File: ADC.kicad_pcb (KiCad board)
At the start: 2 copper layers, 148 parts, among them P1 CONN_6, P10 CONN_2, P11 CONN_2, P12 CONN_2, P13 CONN_4, P14 CONN_2, P15 CONN_2, P16 CONN_2, P17 CONN_4, P2 CONN_6, P3 CONN_6, P4 CONN_6, P5 CONN_1, P6 CONN_2, P7 CONN_2, P8 CONN_2, P9 CONN_2, Q1 BD241A, Q2 BD241A, Q3 BD242, T1 TRIAD-FS16-400-C2, T2 TRIAD-FS48-750-C2, U1 OPA209-SOT23, U12 MC7805C, U13 LM7818CT, U14 LM7918CT, U15 LME49740, U16 LME49740, U2 OPA209-SOT23, U3 OPA209-SOT23, U4 2N6507, U5 2N6507, U6 2N6507, U7 REF02, U8 2N6507, U9 OPA209-SOT23

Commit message: Changed to use the fixed IEC socket device; the PSU netlist should now be (more) correct.
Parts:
- added C21: C, Capacitors_ThroughHole:Capacitor12MMDiscRM7.75, F.Cu at (56.3, 104.6)
- added C22: C, Capacitors_ThroughHole:Capacitor12MMDiscRM7.75, F.Cu at (43.3, 104.6)
- added F1: FUSE, Oddities:Dummy_Empty, F.Cu at (102.6, 105.8)
- added J1: RCA, Oddities:Dummy_Empty, F.Cu at (575.6, 90.6)
- added J2: RCA, Oddities:Dummy_Empty, F.Cu at (623.8, 62.6)
- added J3: IEC-C13-SOCKET, Oddities:Dummy_Empty, F.Cu at (28.0, 103.2)
- added P18: CONN_1, Connect:1pin, F.Cu at (111.8, 26.7)
- added P19: CONN_1, Connect:1pin, F.Cu at (90.2, -113.0)
- added P20: CONN_1, Connect:1pin, F.Cu at (90.2, -123.2)
- added P21: CONN_1, Connect:1pin, F.Cu at (88.9, -143.5)
- added P22: CONN_1, Connect:1pin, F.Cu at (90.2, -154.9)
- added R21: R, Resistors_ThroughHole:Resistor_Horizontal_RM15mm, F.Cu at (96.4, 84.2)
- added R22: R, Resistors_ThroughHole:Resistor_Horizontal_RM15mm, F.Cu at (137.3, 48.1)
- added U10: P0300ECL, Housings_TO-92:TO-92-Free-inline-wide, F.Cu at (93.1, 96.8)
- added U11: P0300ECL, Housings_TO-92:TO-92-Free-inline-wide, F.Cu at (127.1, 62.3)
- P14, P15, P16, P6, P7: footprint Sockets_MOLEX_KK-System:Socket_MOLEX-KK-RM2-54mm_Lock_2pin_straight -> Oddities:Dummy_Empty
- P17: footprint Sockets_MOLEX_KK-System:Socket_MOLEX-KK-RM2-54mm_Lock_4pin_straight -> Oddities:Dummy_Empty
- P2, P3: footprint Sockets_MOLEX_KK-System:Socket_MOLEX-KK-RM2-54mm_Lock_6pin_straight -> Oddities:Dummy_Empty
- moved R33 477.1 mm to (601.5, 6.55)
- moved D20 472.3 mm to (614.1, 6.53)
- moved D23 460.6 mm to (601.0, 27.5)
- moved C40 455.2 mm to (623.2, 6.35)
- moved R34 450.0 mm to (563.4, 27.5)
- moved R41 449.9 mm to (588.8, 6.55)
- moved R39 439.4 mm to (563.4, 6.55)
- moved R50 434.2 mm to (537.8, 6.55)
- moved R46 428.5 mm to (576.2, 6.55)
- moved R48 428.4 mm to (550.6, 6.55)
- moved R44 422.8 mm to (550.6, 38.0)
- moved P12 421.8 mm to (597.9, 64.8)
- moved P8 421.8 mm to (617.4, 64.8)
- moved C41 417.2 mm to (584.5, 47.1)
- moved R32 417.2 mm to (588.7, 17.0)
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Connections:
- T1 pad 1: Net-(J3-Pad~) -> Net-(J3-Pad1)
- T1 pad 2: Net-(J3-Pad~) -> Net-(J3-Pad2)
- T1 pad 3: Net-(J3-Pad~) -> Net-(J3-Pad3)
- T1 pad 4: Net-(J3-Pad~) -> Net-(J3-Pad4)
- T2 pad 1: Net-(J3-Pad~) -> Net-(J3-Pad1)
- T2 pad 2: Net-(J3-Pad~) -> Net-(J3-Pad2)
- T2 pad 3: Net-(J3-Pad~) -> Net-(J3-Pad3)
- T2 pad 4: Net-(J3-Pad~) -> Net-(J3-Pad4)

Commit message: A lot of routing, some parts changes:   * Added snubber C/RC snubbers to transformer secondaries.   * Changed PSU OA from OPA209 to OPA27.   * Routed external PSU.   * Mostly done routing internal circuits.  Just need to get everything together.   * Changed digital transformer to a more appropriately-specced one.
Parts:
- added C44: 470n, Capacitors_ThroughHole:Capacitor3MMDiscRM2.5, F.Cu at (245.4, 51.1)
- added C45: 470n, Capacitors_ThroughHole:Capacitor3MMDiscRM2.5, F.Cu at (248.0, 66.4)
- added HS: Heatsink_Fischer_SK104-STC-STIC_35x13mm_2xDrill2.5mm, Heatsinks:Heatsink_Fischer_SK104-STC-STIC_35x13mm_2xDrill2.5mm, F.Cu at (128.2, 59.9)
- added HS: Heatsink_Fischer_SK104-STC-STIC_35x13mm_2xDrill2.5mm, Heatsinks:Heatsink_Fischer_SK104-STC-STIC_35x13mm_2xDrill2.5mm, F.Cu at (41.9, 48.4)
- added HS: Heatsink_Fischer_SK104-STC-STIC_35x13mm_2xDrill2.5mm, Heatsinks:Heatsink_Fischer_SK104-STC-STIC_35x13mm_2xDrill2.5mm, F.Cu at (78.7, 48.4)
- added HS: Heatsink_Fischer_SK104-STC-STIC_35x13mm_2xDrill2.5mm, Heatsinks:Heatsink_Fischer_SK104-STC-STIC_35x13mm_2xDrill2.5mm, F.Cu at (231.5, 114.0)
- added HS: Heatsink_Fischer_SK104-STC-STIC_35x13mm_2xDrill2.5mm, Heatsinks:Heatsink_Fischer_SK104-STC-STIC_35x13mm_2xDrill2.5mm, F.Cu at (430.5, 181.6)
- added HS: Heatsink_Fischer_SK104-STC-STIC_35x13mm_2xDrill2.5mm, Heatsinks:Heatsink_Fischer_SK104-STC-STIC_35x13mm_2xDrill2.5mm, F.Cu at (177.5, 114.0)
- added MH: MountingHole_5mm_RevA_Date21Jun2010, Mounting_Holes:MountingHole_5mm, F.Cu at (32.5, 35.0)
- added MH: MountingHole_5mm_RevA_Date21Jun2010, Mounting_Holes:MountingHole_5mm, F.Cu at (127.5, 35.0)
- added MH: MountingHole_5mm_RevA_Date21Jun2010, Mounting_Holes:MountingHole_5mm, F.Cu at (32.5, 180.0)
- added MH: MountingHole_5mm_RevA_Date21Jun2010, Mounting_Holes:MountingHole_5mm, F.Cu at (127.5, 180.0)
- added MH: MountingHole_5mm_RevA_Date21Jun2010, Mounting_Holes:MountingHole_5mm, F.Cu at (100.0, 90.0)
- added Sym: Symbol_Highvoltage_Type2_CopperTop_Small, Footprint_Symbols:Symbol_Highvoltage_Type2_CopperTop_Small, B.Cu at (35.6, 138.4)
- added Sym: Symbol_Danger_CopperTop_Big, Footprint_Symbols:Symbol_Danger_CopperTop_Big, B.Cu at (55.9, 137.2)
- C21: value C -> 150n; footprint Capacitors_ThroughHole:Capacitor12MMDiscRM7.75 -> Capacitors_ThroughHole:Capacitor18x6RM15
- C22: value C -> 10n; footprint Capacitors_ThroughHole:Capacitor12MMDiscRM7.75 -> Capacitors_ThroughHole:Capacitor13x4RM10
- C23: value 2700u -> 150n; footprint Capacitors_ThroughHole:Capacitor16x25RM7.5 -> Capacitors_ThroughHole:Capacitor18x6RM15
- C24: value 2700u -> 10n; footprint Capacitors_ThroughHole:Capacitor16x25RM7.5 -> Capacitors_ThroughHole:Capacitor13x4RM10
- C28, C29: value 470n -> 2700u; footprint Capacitors_ThroughHole:Capacitor3MMDiscRM2.5 -> Capacitors_ThroughHole:Capacitor16x25RM7.5
- C31, C32: value 1u -> 470n; footprint Capacitors_ThroughHole:Capacitor5x6RM2.5 -> Capacitors_ThroughHole:Capacitor3MMDiscRM2.5
- C34, C35: value 6.2n -> 1u; footprint Capacitors_ThroughHole:Capacitor18x7RM15 -> Capacitors_ThroughHole:Capacitor5x6RM2.5
- C36, C37: value 22u -> 6.2n; footprint Capacitors_ThroughHole:Capacitor5x11RM2.5 -> Capacitors_ThroughHole:Capacitor18x7RM15
- C38, C39: value 47u -> 22u; footprint Capacitors_Elko_ThroughHole:Elko_vert_DM5_RM2 -> Capacitors_ThroughHole:Capacitor5x11RM2.5
- C40, C41: value 470n -> 47u; footprint Capacitors_ThroughHole:Capacitor3MMDiscRM2.5 -> Capacitors_Elko_ThroughHole:Elko_vert_DM5_RM2
- T1: value TRIAD-FS16-400-C2 -> TRIAD-FS20-300-C2
- U1, U2, U3, U9: value OPA209-SOT23 -> OPA27; footprint SMD_Packages:SOT23-5 -> Sockets_DIP:DIP-8__300_ELL
- moved J3 767.8 mm to (793.7, 160.3)
- moved F1 687.6 mm to (787.5, 167.1)
- moved C40 446.9 mm to (180.3, 66.0)
- moved C35 446.3 mm to (45.7, 63.7), turned to 270 degrees
- moved C42 423.9 mm to (189.2, 64.8)
- moved D19 421.2 mm to (180.3, 30.5), turned to 180 degrees
- moved P8 415.1 mm to (202.6, 80.0), turned to 90 degrees
- moved P5 411.9 mm to (177.8, 153.0)
- moved C43 410.8 mm to (186.7, 49.5)
- moved R32 409.4 mm to (180.3, 45.7)
- moved C34 407.4 mm to (82.5, 63.7), turned to 90 degrees
- moved R33 406.9 mm to (196.8, 49.5)
- moved R31 396.0 mm to (180.3, 41.9)
- moved D17 395.5 mm to (180.3, 34.3)
- moved P10 395.4 mm to (202.6, 69.8), turned to 90 degrees
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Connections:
- net Net-(J3-Pad1) renamed /PSU-external/PA1
- net Net-(J3-Pad2) renamed /PSU-external/PA2
- net Net-(J3-Pad3) renamed /PSU-external/PB1
- net Net-(J3-Pad4) renamed /PSU-external/PB2
- C21 pad 1: Net-(C21-Pad1) -> /PSU-external/SEC4
- C21 pad 2: Net-(C21-Pad2) -> /PSU-external/SEC3
- C22 pad 1: Net-(C22-Pad1) -> /PSU-external/SEC6
- C22 pad 2: Net-(C22-Pad2) -> /PSU-external/SEC3
- C23 pad 1: Net-(C23-Pad1) -> /PSU-external/SEC2
- C23 pad 2: /PSU-external/AGND_EXT -> /PSU-external/SEC1
- C24 pad 1: /PSU-external/AGND_EXT -> /PSU-external/SEC7
- C24 pad 2: Net-(C24-Pad2) -> /PSU-external/SEC1
- C25 pad 2: /PSU-external/DGND_EXT -> /PSU-external/AGND_EXT
- C26 pad 1: Net-(C23-Pad1) -> /PSU-external/AGND_EXT
- C26 pad 2: /PSU-external/AGND_EXT -> Net-(C26-Pad2)
- C27 pad 1: /PSU-external/AGND_EXT -> Net-(C27-Pad1)
- C27 pad 2: Net-(C24-Pad2) -> /PSU-external/DGND_EXT
- C28 pad 2: /PSU-external/DGND_EXT -> /PSU-external/AGND_EXT
- C29 pad 1: Net-(C23-Pad1) -> /PSU-external/AGND_EXT
- C29 pad 2: /PSU-external/AGND_EXT -> Net-(C26-Pad2)
- C30 pad 1: /PSU-external/AGND_EXT -> Net-(C27-Pad1)
- C30 pad 2: Net-(C24-Pad2) -> /PSU-external/DGND_EXT
- C31 pad 1: /PSU-external/+5V_EXT -> Net-(C25-Pad1)
- C31 pad 2: /PSU-external/DGND_EXT -> /PSU-external/AGND_EXT
- C32 pad 1: /PSU-external/+18V_EXT -> /PSU-external/AGND_EXT
- C32 pad 2: /PSU-external/AGND_EXT -> Net-(C26-Pad2)
- C33 pad 1: /PSU-external/AGND_EXT -> /PSU-external/+5V_EXT
- C33 pad 2: /PSU-external/-18V_EXT -> /PSU-external/DGND_EXT
- C34 pad 1: Net-(C34-Pad1) -> /PSU-external/+18V_EXT
- C34 pad 2: /Clipper/AGND -> /PSU-external/AGND_EXT
- C35 pad 1: Net-(C35-Pad1) -> /PSU-external/AGND_EXT
- C35 pad 2: /Clipper/AGND -> /PSU-external/-18V_EXT
- C36 pad 1: Net-(C34-Pad1) -> Net-(C36-Pad1)
- C36 pad 2: Net-(C36-Pad2) -> /Clipper/AGND
- C37 pad 1: Net-(C35-Pad1) -> Net-(C37-Pad1)
- C37 pad 2: Net-(C37-Pad2) -> /Clipper/AGND
- C38 pad 1: /Clipper/LIN -> Net-(C36-Pad1)
- C39 pad 1: /Clipper/RIN -> Net-(C37-Pad1)
- C40 pad 1: /Clipper/+15V -> /Clipper/LIN
- C40 pad 2: /Clipper/AGND -> Net-(C40-Pad2)
- C41 pad 1: /Clipper/AGND -> /Clipper/RIN
- C41 pad 2: /Clipper/-15V -> Net-(C41-Pad2)
- D10 pad 2: Net-(D10-Pad2) -> /PSU-external/SEC4
- D11 pad 1: Net-(C22-Pad2) -> /PSU-external/SEC1
- D11 pad 2: Net-(C23-Pad1) -> Net-(C25-Pad1)
- D12 pad 1: Net-(C24-Pad2) -> Net-(C26-Pad2)
- D12 pad 2: Net-(C22-Pad2) -> /PSU-external/SEC1
- D13 pad 2: Net-(C25-Pad1) -> Net-(C27-Pad1)
- D14 pad 2: Net-(C23-Pad1) -> Net-(C25-Pad1)
- D15 pad 1: Net-(C24-Pad2) -> Net-(C26-Pad2)
- D19 pad 1: Net-(D17-Pad2) -> Net-(D19-Pad1)
- D19 pad 2: Net-(D19-Pad2) -> Net-(D17-Pad1)
- D23 pad 1: Net-(D21-Pad2) -> Net-(D23-Pad1)
- D23 pad 2: Net-(D23-Pad2) -> Net-(D21-Pad1)
- D5 pad 1: Net-(C21-Pad2) -> /PSU-external/SEC3
- D5 pad 2: Net-(C25-Pad1) -> Net-(C27-Pad1)
- D6 pad 2: Net-(C21-Pad2) -> /PSU-external/SEC3
- D7 pad 1: Net-(D7-Pad1) -> /PSU-external/SEC2
- D7 pad 2: Net-(C23-Pad1) -> Net-(C25-Pad1)
- D8 pad 1: Net-(C24-Pad2) -> Net-(C26-Pad2)
- D8 pad 2: Net-(D7-Pad1) -> /PSU-external/SEC2
- D9 pad 1: Net-(D10-Pad2) -> /PSU-external/SEC4
- D9 pad 2: Net-(C25-Pad1) -> Net-(C27-Pad1)
- P1 pad 1: /PSU-external/SAF_GND -> /PSU-external/+5V_EXT
- P1 pad 2: /PSU-external/+5V_EXT -> /PSU-external/DGND_EXT
- P1 pad 3: /PSU-external/DGND_EXT -> /PSU-external/SAF_GND
- P4 pad 1: Net-(P4-Pad1) -> /PSU-internal/+5V
- P4 pad 2: /PSU-internal/+5V -> /PSU-internal/DGND
- P4 pad 3: /PSU-internal/DGND -> Net-(P4-Pad3)
- P5 pad 1: Net-(P4-Pad1) -> Net-(P4-Pad3)
- R21 pad 1: Net-(C21-Pad1) -> /PSU-external/SEC6
- R21 pad 2: Net-(D10-Pad2) -> /PSU-external/SEC4
- R22 pad 1: Net-(C22-Pad1) -> /PSU-external/SEC7
- R22 pad 2: Net-(D7-Pad1) -> /PSU-external/SEC2
- R23 pad 2: Net-(C34-Pad1) -> Net-(C36-Pad1)
- R24 pad 2: Net-(C35-Pad1) -> Net-(C37-Pad1)
- R25 pad 1: Net-(C34-Pad1) -> Net-(C36-Pad1)
- R26 pad 1: Net-(C35-Pad1) -> Net-(C37-Pad1)
- R27 pad 1: Net-(C36-Pad2) -> Net-(C38-Pad2)
- R28 pad 1: Net-(C37-Pad2) -> Net-(C39-Pad2)
- R32 pad 2: Net-(D17-Pad1) -> Net-(D17-Pad2)
- R34 pad 2: Net-(D17-Pad1) -> Net-(D17-Pad2)
- R36 pad 1: Net-(D17-Pad1) -> Net-(D17-Pad2)
- R36 pad 2: Net-(D19-Pad2) -> Net-(D19-Pad1)
- R39 pad 1: Net-(D19-Pad2) -> Net-(D19-Pad1)
- R42 pad 2: Net-(D21-Pad1) -> Net-(D21-Pad2)
- R44 pad 2: Net-(D21-Pad1) -> Net-(D21-Pad2)
- R46 pad 1: Net-(D21-Pad1) -> Net-(D21-Pad2)
- R46 pad 2: Net-(D23-Pad2) -> Net-(D23-Pad1)
- R49 pad 1: Net-(D23-Pad2) -> Net-(D23-Pad1)
- T1 pad 5: Net-(C21-Pad2) -> /PSU-external/SEC3
- T1 pad 6: Net-(T1-Pad6) -> /PSU-external/SEC4
- T1 pad 7: Net-(T1-Pad6) -> /PSU-external/SEC3
- T1 pad 8: Net-(D10-Pad2) -> /PSU-external/SEC4
- T2 pad 5: Net-(C22-Pad2) -> /PSU-external/SEC1
- T2 pad 8: Net-(D7-Pad1) -> /PSU-external/SEC2
- U1 pad 1: Net-(R11-Pad2) -> Net-(U1-Pad1)
- U1 pad 2: /Clipper/AGND -> Net-(C4-Pad2)
- U1 pad 4: Net-(C4-Pad2) -> /PSU-internal/-18V_EXT
- U1 pad 5: /PSU-internal/+18V_EXT -> (no net)
- U10 pad 1: Net-(T1-Pad6) -> /PSU-external/SEC3
- U12 pad 1: Net-(C25-Pad1) -> Net-(C27-Pad1)
- U13 pad 1: Net-(C23-Pad1) -> Net-(C25-Pad1)
- U14 pad 2: Net-(C24-Pad2) -> Net-(C26-Pad2)
- U15 pad 1: Net-(C38-Pad2) -> Net-(C40-Pad2)
- U15 pad 13: Net-(R37-Pad2) -> Net-(D17-Pad2)
- U15 pad 14: /Clipper/LOUT -> Net-(D17-Pad1)
- U15 pad 2: Net-(C38-Pad2) -> Net-(C40-Pad2)
- U15 pad 3: Net-(C36-Pad2) -> Net-(C38-Pad2)
- U15 pad 6: Net-(D17-Pad1) -> Net-(R37-Pad2)
- U15 pad 7: Net-(D17-Pad2) -> /Clipper/LOUT
- U16 pad 1: Net-(C39-Pad2) -> Net-(C41-Pad2)
- U16 pad 13: Net-(R47-Pad2) -> Net-(D21-Pad2)
- U16 pad 14: /Clipper/ROUT -> Net-(D21-Pad1)
- U16 pad 2: Net-(C39-Pad2) -> Net-(C41-Pad2)
- U16 pad 3: Net-(C37-Pad2) -> Net-(C39-Pad2)
- U16 pad 6: Net-(D21-Pad1) -> Net-(R47-Pad2)
- U16 pad 7: Net-(D21-Pad2) -> /Clipper/ROUT
- U2 pad 1: Net-(R12-Pad2) -> Net-(U2-Pad1)
- U2 pad 2: /Clipper/AGND -> Net-(C5-Pad2)
- U2 pad 4: Net-(C5-Pad2) -> /PSU-internal/-18V_EXT
- U2 pad 5: /PSU-internal/+18V_EXT -> (no net)
- U3 pad 1: Net-(R13-Pad2) -> Net-(U3-Pad1)
- U3 pad 2: /PSU-internal/-18V_EXT -> Net-(C6-Pad1)
- U3 pad 4: Net-(C6-Pad1) -> /PSU-internal/-18V_EXT
- U3 pad 5: /Clipper/AGND -> (no net)
- U9 pad 1: /PSU-internal/VREF- -> Net-(U9-Pad1)
- U9 pad 2: /PSU-internal/-18V_EXT -> Net-(R18-Pad1)
- U9 pad 4: Net-(R18-Pad1) -> /PSU-internal/-18V_EXT
- U9 pad 5: /PSU-internal/+18V_EXT -> (no net)
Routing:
- net /PSU-external/AGND_EXT: track 0.00 -> 287.6 mm, vias 0 -> 4
- net /PSU-external/SAF_GND: track 0.00 -> 191.5 mm
- net /PSU-external/PA1: track 0.00 -> 147.9 mm
- net /PSU-external/DGND_EXT: track 0.00 -> 122.7 mm
- net Net-(C26-Pad2): track 0.00 -> 119.6 mm
- net Net-(C25-Pad1): track 0.00 -> 109.4 mm
- net /PSU-external/PA2: track 0.00 -> 105.2 mm
- net /Clipper/+15V: track 0.00 -> 97.3 mm
- net /PSU-external/+5V_EXT: track 0.00 -> 85.1 mm
- net /PSU-internal/-18V_EXT: track 0.00 -> 82.6 mm
- net /PSU-external/SEC3: track 0.00 -> 80.8 mm
- net /PSU-external/PB1: track 0.00 -> 78.8 mm
- net /PSU-internal/+18V_EXT: track 0.00 -> 78.3 mm
- net /Clipper/-15V: track 0.00 -> 78.1 mm
- net Net-(C27-Pad1): track 0.00 -> 75.6 mm
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- added copper zone on B.Cu, net /PSU-external/SAF_GND
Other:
- board outline added: 247.5 x 165 mm
- net class Default: trace_width 0.254 -> 1
- net class HighVoltage added: clearance 1, trace_width 2, via_dia 0.889, via_drill 0.635
- net class Power added: clearance 0.254, trace_width 1, via_dia 0.889, via_drill 0.635

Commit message: First complete version.   * Added 10uF decoupling capacitors to the start of each signal processing section.   * Completed routing.  A few -18 V nets remain unrouted; these will be wired in.
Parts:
- added C46: 10u, Capacitors_Elko_ThroughHole:Elko_vert_DM5_RM2-5, F.Cu at (207.0, 64.1)
- added C47: 10u, Capacitors_Elko_ThroughHole:Elko_vert_DM5_RM2-5, F.Cu at (205.1, 122.6)
- added MH: MountingHole_5mm_RevA_Date21Jun2010, Mounting_Holes:MountingHole_5mm, F.Cu at (263.8, 100.5)
- added MH: MountingHole_5mm_RevA_Date21Jun2010, Mounting_Holes:MountingHole_5mm, F.Cu at (181.3, 155.5)
- added MH: MountingHole_5mm_RevA_Date21Jun2010, Mounting_Holes:MountingHole_5mm, F.Cu at (261.3, 155.5)
- added MH: MountingHole_5mm_RevA_Date21Jun2010, Mounting_Holes:MountingHole_5mm, F.Cu at (181.3, 25.5)
- added MH: MountingHole_5mm_RevA_Date21Jun2010, Mounting_Holes:MountingHole_5mm, F.Cu at (226.3, 25.5)
- R1, R10, R11, R12, R13, R18, R2, R3, R5, R6, R8, R9: footprint Resistors_ThroughHole:Resistor_Horizontal_RM10mm -> Resistors_ThroughHole:Resistor_Vertical_RM5mm
- moved P13 342.7 mm to (221.0, 41.3), turned to 180 degrees
- moved R15 255.0 mm to (240.7, 57.8)
- moved D2 250.6 mm to (240.7, 61.6)
- moved C11 239.3 mm to (249.6, 59.1)
- moved C8 238.3 mm to (236.2, 85.1), turned to 90 degrees
- moved C2 233.2 mm to (236.2, 76.8), turned to 270 degrees
- moved R4 231.4 mm to (231.1, 73.0), turned to 90 degrees
- moved C5 220.8 mm to (250.2, 81.9), turned to 90 degrees
- moved R6 216.5 mm to (244.5, 83.8), turned to 90 degrees
- moved R2 216.4 mm to (236.2, 69.8)
- moved U2 216.1 mm to (247.0, 73.7), turned to 270 degrees
- moved C17 214.5 mm to (247.0, 65.4), turned to 180 degrees
- moved R9 209.8 mm to (255.9, 84.5), turned to 270 degrees
- moved U5 204.4 mm to (254.0, 62.9), turned to 270 degrees
- moved R12 203.8 mm to (255.9, 74.9), turned to 270 degrees
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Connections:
- C13 pad 1: /Clipper/+15V -> /PSU-internal/+18V_EXT
- R3 pad 1: Net-(C6-Pad1) -> /Clipper/AGND
- R3 pad 2: /Clipper/AGND -> Net-(C6-Pad1)
- U7 pad 2: /Clipper/+15V -> /PSU-internal/+18V_EXT
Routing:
- net /PSU-internal/+18V_EXT: track 78.3 -> 397.6 mm, vias 0 -> 4
- net /Clipper/-15V: track 78.1 -> 379.1 mm, vias 0 -> 8
- net /Clipper/+15V: track 97.3 -> 350.0 mm
- net /Clipper/AGND: track 0.00 -> 162.8 mm
- net /PSU-internal/+4V: track 42.1 -> 174.0 mm, vias 0 -> 4
- net /PSU-internal/DGND: track 43.3 -> 138.9 mm
- net /PSU-internal/-18V_EXT: track 82.6 -> 166.4 mm, vias 0 -> 6
- net /PSU-internal/VREF+: track 0.00 -> 82.6 mm
- net Net-(C11-Pad1): track 62.1 -> 12.6 mm
- net Net-(C10-Pad1): track 58.2 -> 12.4 mm
- net Net-(C12-Pad1): track 59.4 -> 22.0 mm
- net /PSU-internal/+5V: track 60.1 -> 87.4 mm
- net /PSU-internal/VREF-: track 0.00 -> 21.3 mm
- net Net-(R18-Pad1): track 0.00 -> 19.0 mm
- net Net-(C4-Pad2): track 42.1 -> 26.9 mm
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- added copper zone on F.Cu, net /Clipper/AGND
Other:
- board size 247.5 x 165 mm -> 248.8 x 174.5 mm
- copper layers 2 -> 4
- net class Default: via_dia 0.889 -> 2; via_drill 0.635 -> 1
- net class HighVoltage: via_dia 0.889 -> 2; via_drill 0.635 -> 1
- net class Power: via_dia 0.889 -> 2; via_drill 0.635 -> 1

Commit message: Routed the -18 V line, added licence and descriptive text.
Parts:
- removed F1: FUSE, Oddities:Dummy_Empty
- removed J1, J2: RCA, Oddities:Dummy_Empty
- removed J3: IEC-C13-SOCKET, Oddities:Dummy_Empty
- removed the MH at (263.8, 100.5)
- removed the MH at (181.3, 155.5)
- removed the MH at (261.3, 155.5)
- removed the MH at (181.3, 25.5)
- removed the MH at (226.3, 25.5)
- removed P14, P15, P16, P6, P7: CONN_2, Oddities:Dummy_Empty
- removed P17: CONN_4, Oddities:Dummy_Empty
- removed P2, P3: CONN_6, Oddities:Dummy_Empty
- removed the Sym at (55.9, 137.2)
- added FID: Fiducial_Modern_CopperBottom_RevC, Fiducials:Fiducial_Modern_CopperBottom, F.Cu at (175.0, 20.0)
- added FID: Fiducial_Modern_CopperBottom_RevC, Fiducials:Fiducial_Modern_CopperBottom, F.Cu at (265.0, 160.0)
- added FID: Fiducial_Modern_CopperBottom_RevC, Fiducials:Fiducial_Modern_CopperBottom, F.Cu at (175.0, 160.0)
- added MH: MountingHole_3mm_RevA_Date21Jun2010, Mounting_Holes:MountingHole_3mm, F.Cu at (260.0, 155.0)
- added MH: MountingHole_3mm_RevA_Date21Jun2010, Mounting_Holes:MountingHole_3mm, F.Cu at (180.0, 155.0)
- added MH: MountingHole_3mm_RevA_Date21Jun2010, Mounting_Holes:MountingHole_3mm, F.Cu at (180.0, 25.0)
- added MH: MountingHole_3mm_RevA_Date21Jun2010, Mounting_Holes:MountingHole_3mm, F.Cu at (222.5, 25.0)
- added MH: MountingHole_3mm_RevA_Date21Jun2010, Mounting_Holes:MountingHole_3mm, F.Cu at (177.5, 90.0)
- added MH: MountingHole_3mm_RevA_Date21Jun2010, Mounting_Holes:MountingHole_3mm, F.Cu at (262.5, 97.5)
- moved Sym 15.6 mm to (50.0, 132.5)
- moved P19 11.2 mm to (132.0, 155.3)
- moved C21 11.2 mm to (130.7, 95.6)
- moved C22 11.2 mm to (116.7, 91.8)
- moved C23 11.2 mm to (69.7, 95.6)
- moved C24 11.2 mm to (55.8, 91.8)
- moved C25 11.2 mm to (91.3, 66.4)
- moved C26 11.2 mm to (58.3, 66.4)
- moved C27 11.2 mm to (114.2, 61.3)
- moved C28 11.2 mm to (74.8, 66.4)
- moved C29 11.2 mm to (41.8, 66.4)
- moved C30 11.2 mm to (115.5, 39.7)
- moved C31 11.2 mm to (79.9, 53.7)
- moved C32 11.2 mm to (43.1, 53.7)
- moved C33 11.2 mm to (115.5, 47.3)
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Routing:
- net /PSU-internal/-18V_EXT: track 166.4 -> 375.3 mm, vias 6 -> 10
- net /Clipper/AGND: track 162.8 -> 61.3 mm
- net /Clipper/-15V: track 379.1 -> 390.2 mm
- net /Clipper/+15V: track 350.0 -> 356.3 mm
- net /PSU-internal/+18V_EXT: track 397.6 -> 401.5 mm, vias 4 -> 6
- net Net-(C2-Pad1): track 22.3 -> 20.3 mm
- net Net-(C5-Pad2): track 27.7 -> 25.7 mm
- net Net-(C3-Pad2): track 12.5 -> 14.3 mm
- net /PSU-internal/VREF-: track 21.3 -> 22.6 mm
- net /PSU-internal/+4V: track 174.0 -> 172.8 mm
- net /PSU-internal/VREF+: track 82.6 -> 83.8 mm
- net Net-(C36-Pad1): track 18.4 -> 19.5 mm
- net Net-(C37-Pad1): track 18.4 -> 19.4 mm
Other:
- board size 248.8 x 174.5 mm -> 242.5 x 165 mm
- board text added: "1 of 1"
- board text added: "1.0"
- board text added: "3 June 2014"
- board text added: "ADC1 PSU-A v1.0 M Pinese 2014 (CC) BY-SA 4.0"
- board text added: "ADC1 PSU-B/Sig v1.0 M Pinese 2014 (CC) BY-SA 4.0"
- board text added: "ADC1: External PSU, internal PSU, and signal processing circuitry. Designed for use with TI PCM4222EVM ADC board. v1.0 (C) Mark Pinese 2014 Design licensed under Creative Commons BY-SA v4.0 http://creativecommons.org/licenses/by-sa/4.0/"
- board text added: "Layer F.Cu on board PSU-A represents wire links. Layer Inner2.Cu on board PSU-B/Sig represents wire links. Use insulated screws for PSU-A."
- board text added: "PCM4222EVM ADC1: Power supply and signal circuitry"

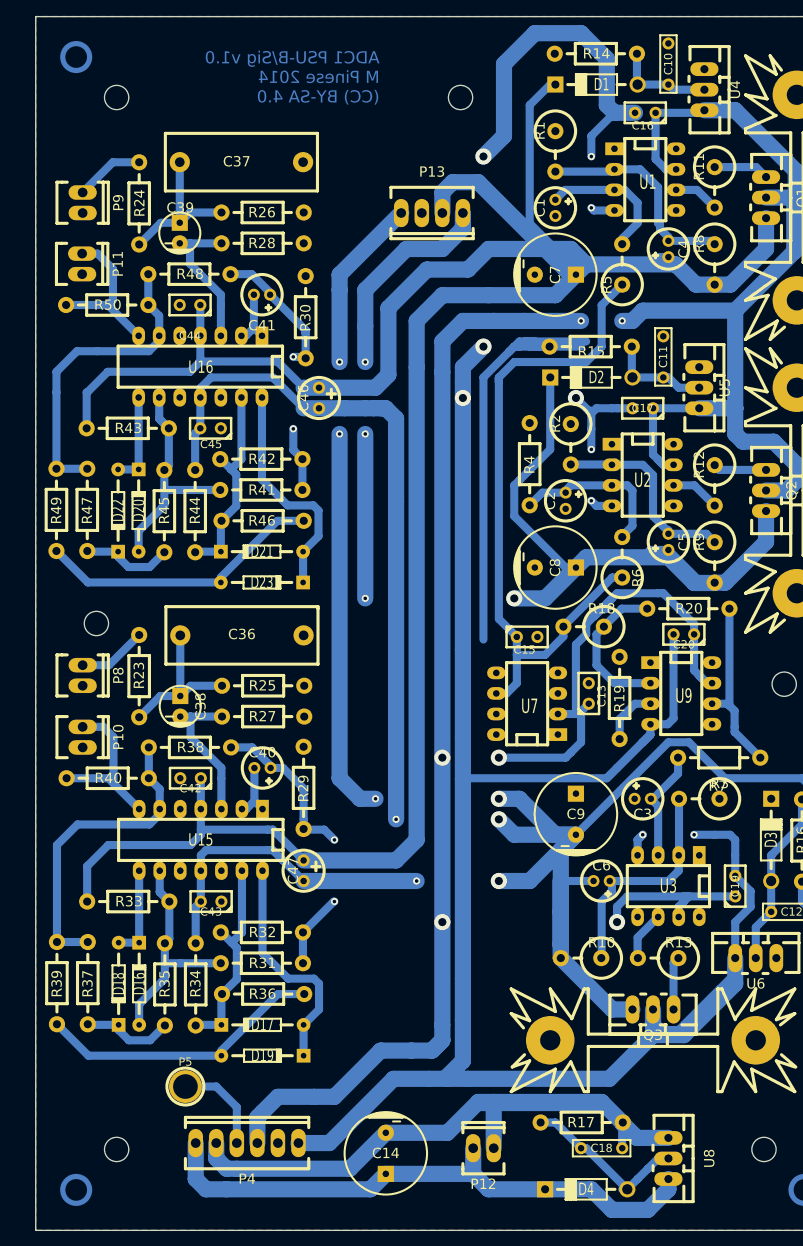
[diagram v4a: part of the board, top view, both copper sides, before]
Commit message: Added vias for ground-connected pins that cannot be soldered from the top, as I can't make PTHs. Rearranged the power inputs slightly.
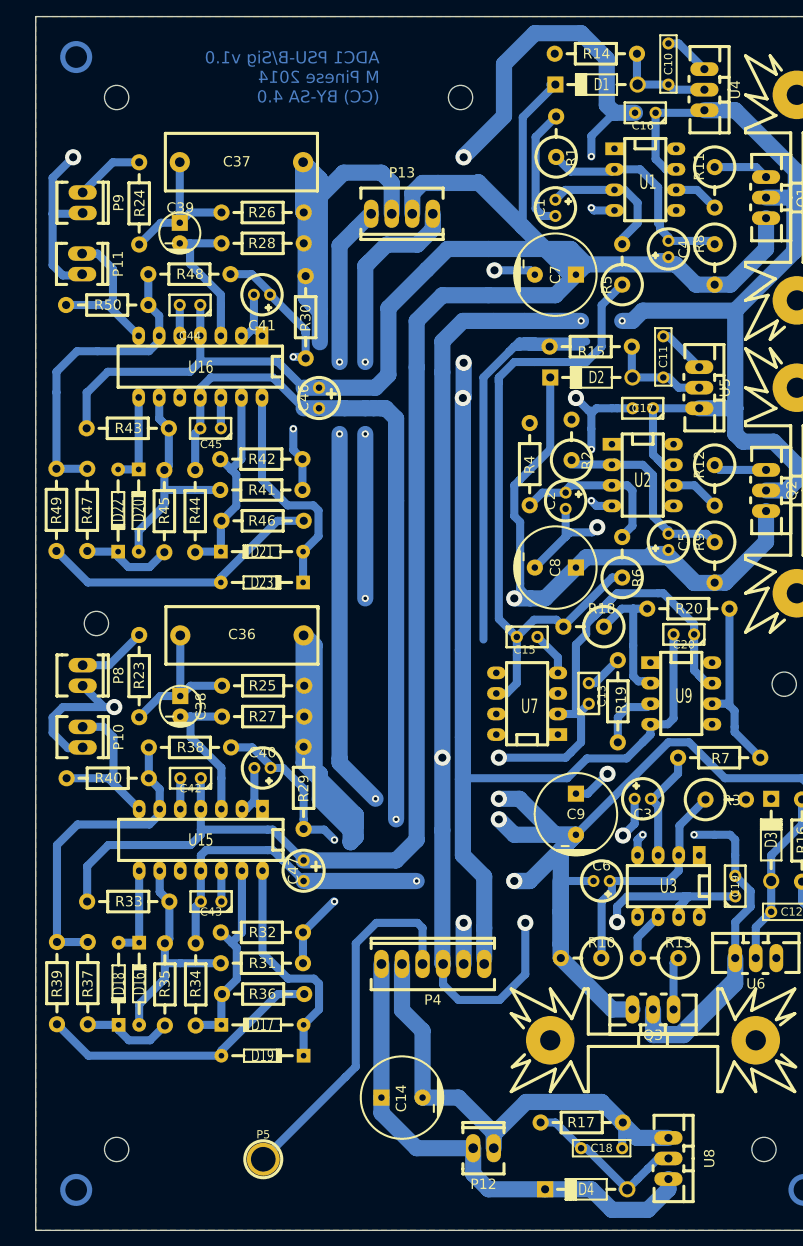
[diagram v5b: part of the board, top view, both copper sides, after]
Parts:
- added F1: FUSE, Oddities:Dummy_Empty, F.Cu at (148.8, 190.1)
- added J1, J2: RCA, Oddities:Dummy_Empty, F.Cu at (148.8, 190.1)
- added J3: IEC-C13-SOCKET, Oddities:Dummy_Empty, F.Cu at (148.8, 190.1)
- added P14, P15, P16, P6, P7: CONN_2, Oddities:Dummy_Empty, F.Cu at (148.8, 190.1)
- added P17: CONN_4, Oddities:Dummy_Empty, F.Cu at (148.8, 190.1)
- added P2, P3: CONN_6, Oddities:Dummy_Empty, F.Cu at (148.8, 190.1)
- moved P4 31.9 mm to (219.1, 132.1)
- moved P5 13.2 mm to (198.1, 156.2)
- moved C14 7.17 mm to (215.3, 148.6), turned to 270 degrees
- moved P13 3.72 mm to (215.3, 39.4)
- moved R3 3.27 mm to (255.3, 111.8), turned to 0 degrees
- moved R1 1.81 mm to (234.3, 29.8), turned to 90 degrees
- moved R2 0.55 mm to (236.2, 67.3), turned to 90 degrees
- moved R19 0.47 mm to (241.9, 99.7)
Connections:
- R1 pad 1: /Clipper/AGND -> Net-(C4-Pad2)
- R1 pad 2: Net-(C4-Pad2) -> /Clipper/AGND
- R2 pad 1: /Clipper/AGND -> Net-(C5-Pad2)
- R2 pad 2: Net-(C5-Pad2) -> /Clipper/AGND
- R3 pad 1: /Clipper/AGND -> Net-(C6-Pad1)
- R3 pad 2: Net-(C6-Pad1) -> /Clipper/AGND
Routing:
- net /Clipper/AGND: track 61.3 -> 342.5 mm, vias 0 -> 7
- net /PSU-internal/DGND: track 138.9 -> 63.9 mm
- net /PSU-internal/-18V_EXT: track 375.3 -> 303.8 mm
- net Net-(P4-Pad3): track 11.8 -> 45.4 mm
- net /PSU-internal/+18V_EXT: track 401.5 -> 371.5 mm
- net /PSU-internal/+5V: track 87.4 -> 78.9 mm
- net Net-(R18-Pad1): track 19.0 -> 17.3 mm
- net Net-(C6-Pad1): track 28.2 -> 29.4 mm
- net /PSU-internal/+4V: track 172.8 -> 171.7 mm
- net /PSU-internal/VREF+: track 83.8 -> 82.9 mm
- net /Clipper/+15V: track 356.3 -> 355.5 mm
- net Net-(R19-Pad1): track 7.06 -> 7.83 mm
- net Net-(C4-Pad2): track 26.9 -> 27.6 mm
- net /Clipper/-15V: track 390.2 -> 389.6 mm
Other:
- net class Power: trace_width 1 -> 2
